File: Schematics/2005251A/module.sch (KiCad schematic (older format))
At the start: 0 parts

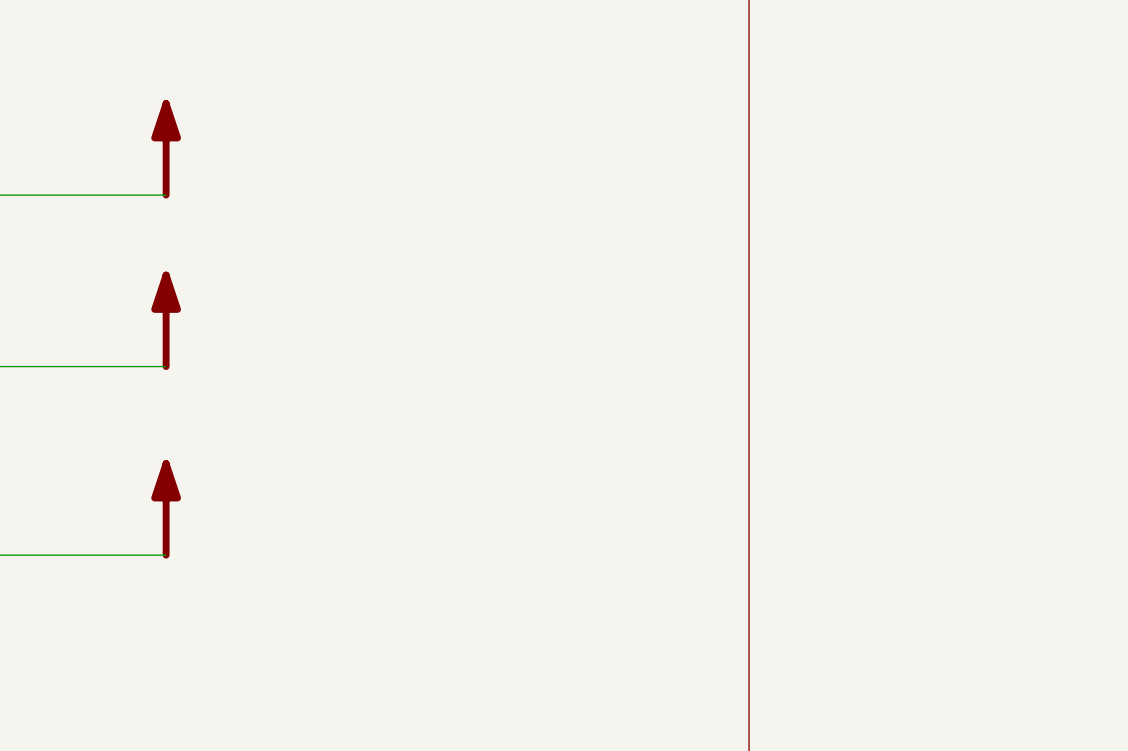
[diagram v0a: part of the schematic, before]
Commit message: Finished up transcribing 2005251A, which is module A3 for AGC's 2003200 and 2003993.
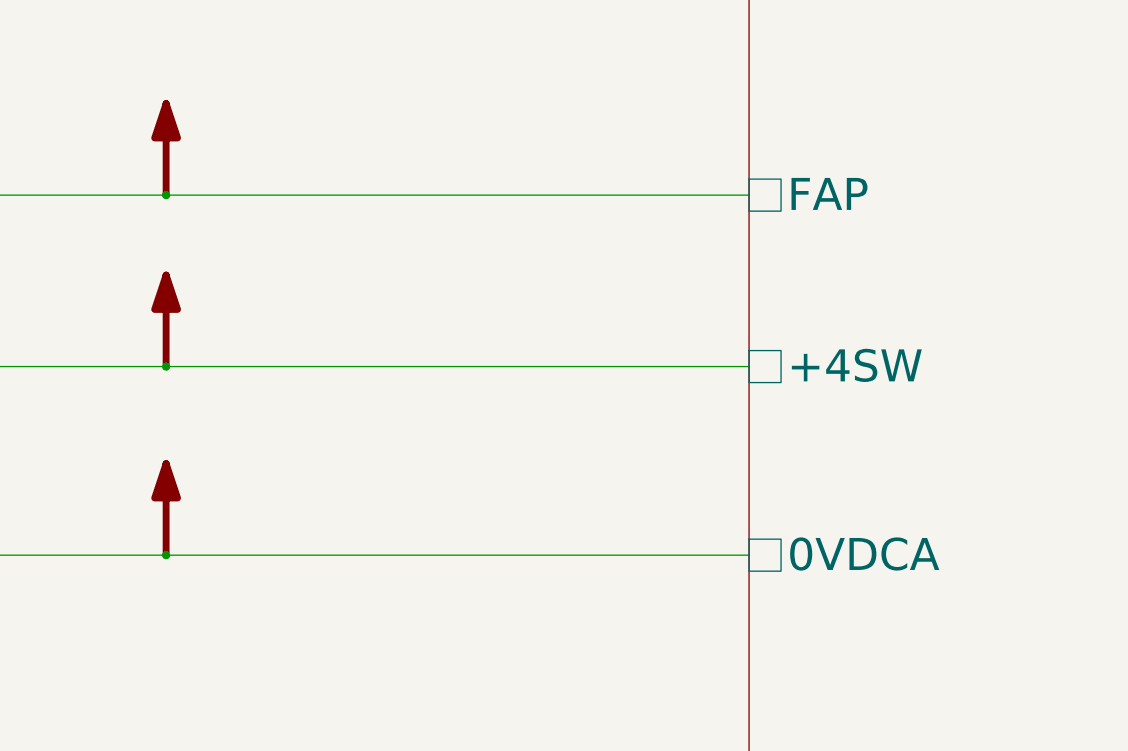
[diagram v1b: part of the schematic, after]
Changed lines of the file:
@@
 F0 "Sheet 2" 140
 F1 "2005251A-p2of2.sch" 140
+F2 "FAP" U L 23900 15000 140
+F3 "0VDCA" U L 23900 16575 140
+F4 "+4SW" U L 23900 15750 140
 $EndSheet
 $Comp
@@
 Text Notes 38425 32450 0    200  ~ 40
 S Q REGISTER  AND  DECODING
+Wire Wire Line
+	21350 15000 23900 15000
+Connection ~ 21350 15000
+Wire Wire Line
+	23900 15750 21350 15750
+Connection ~ 21350 15750
+Wire Wire Line
+	23900 16575 21350 16575
+Connection ~ 21350 16575
 $EndSCHEMATC

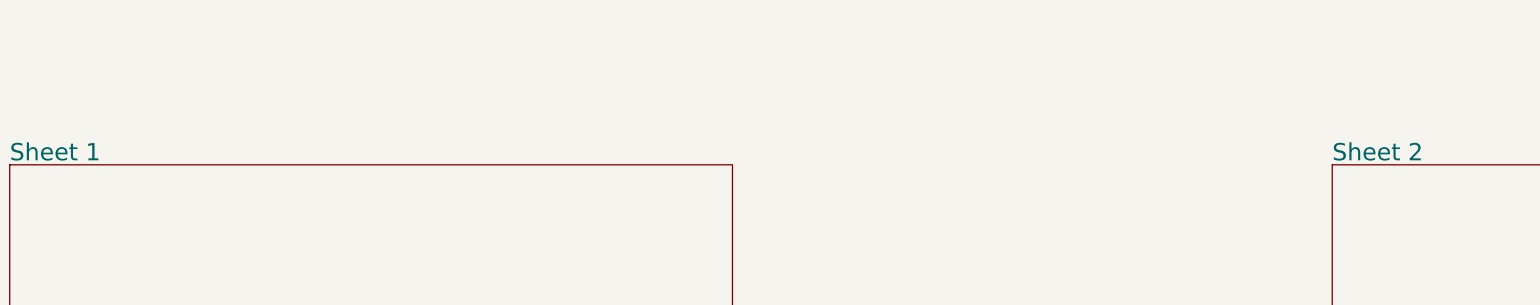
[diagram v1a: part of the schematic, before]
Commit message: Cleaned up and corrected connector captions of 2005251A in CAD vs Mike's database.
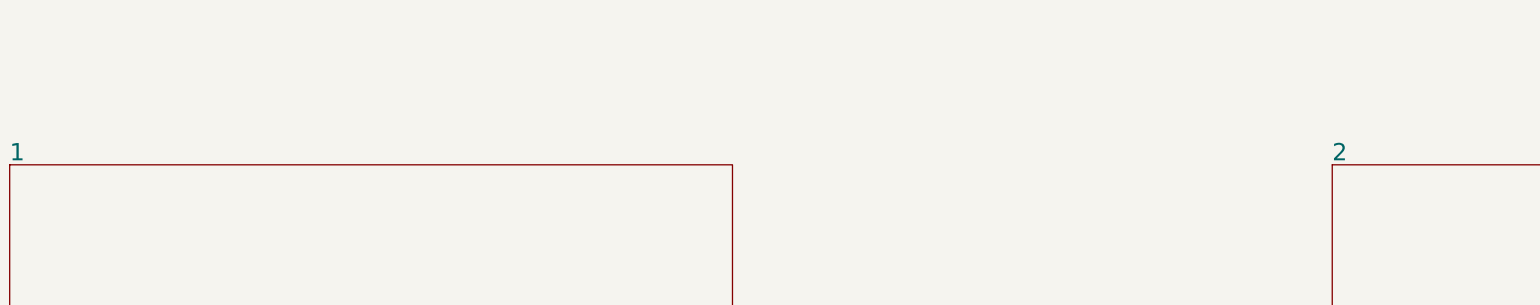
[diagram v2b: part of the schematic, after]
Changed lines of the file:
@@
 S 13150 11250 5875 9375
 U 5B813BEA
-F0 "Sheet 1" 140
+F0 "1" 140
 F1 "2005251A-p1of2.sch" 140
 F2 "+4SW" U R 19025 15750 140
@@
 S 23900 11250 5850 9375
 U 5B813C0D
-F0 "Sheet 2" 140
+F0 "2" 140
 F1 "2005251A-p2of2.sch" 140
 F2 "FAP" U L 23900 15000 140
